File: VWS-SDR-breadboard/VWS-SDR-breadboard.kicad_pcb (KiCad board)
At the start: 4 copper layers, 47 x 30 mm, 78 parts, among them J1 RF_IN, J3 Conn_01x14, U1 GALI-S66, U2 74CBTLV3253DR, U3 MC33078, U4 MC33078, U5 AMS1117-3.3

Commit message: Board cleanup; Updated schematic info block
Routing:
- net GND: track 108.0 -> 106.9 mm
- net Net-(U3B--): track 15.1 -> 14.2 mm
- net Net-(C23-Pad1): track 17.4 -> 16.6 mm
- net Net-(U2-1B1): track 10.0 -> 9.25 mm
- net Net-(U2-1B2): track 8.26 -> 7.55 mm
- net Net-(U4A-+): track 13.2 -> 12.5 mm

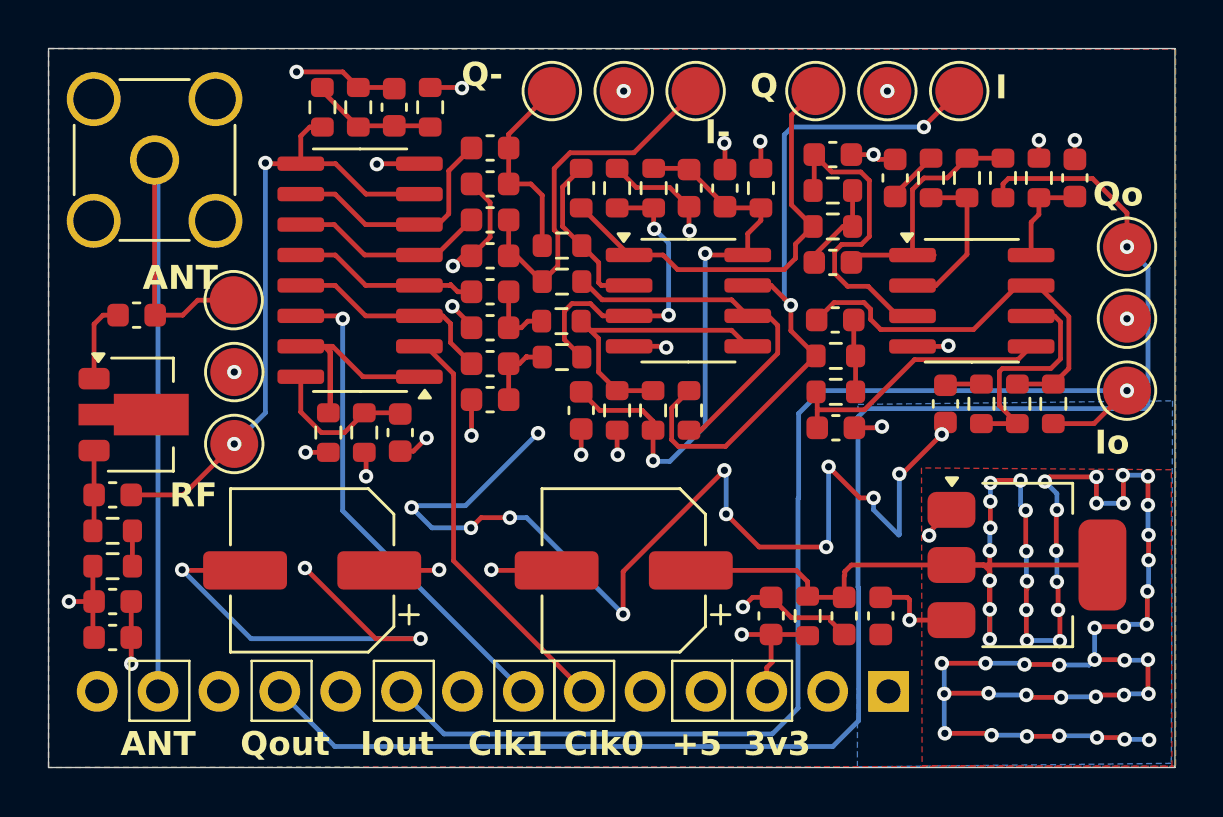
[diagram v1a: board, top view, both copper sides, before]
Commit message: v1.1: - Changed order of pins on the connector to simplify routing. I/Q should be closer to the power pins. clock should be closer to the antenna - Added GND fill on the Vcc layer under the antenna trace to the breadboard connector -Added ground stitching around the RF amp
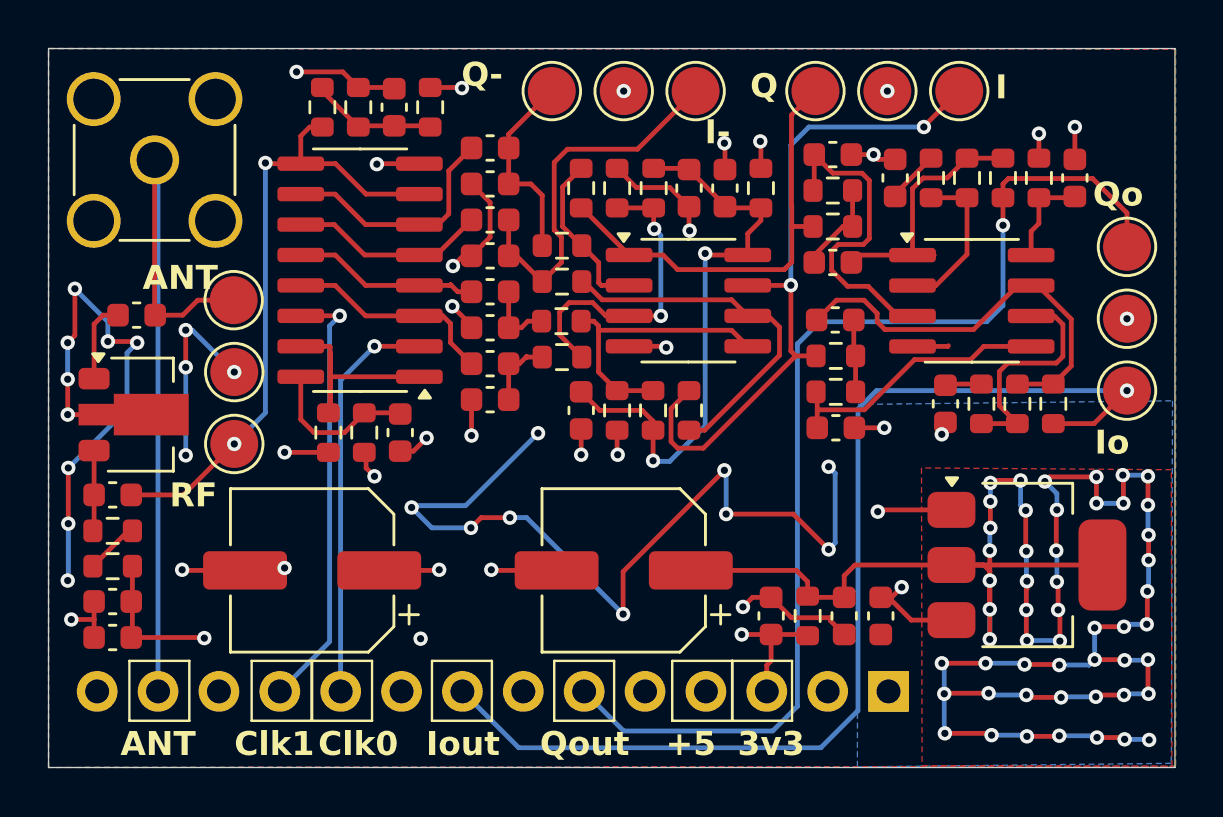
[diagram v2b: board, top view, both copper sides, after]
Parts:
- turned C2 to 0 degrees
- turned C3 to 0 degrees
- turned R1 to 180 degrees
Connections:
- J3 pad 10: GND -> /CLK0
- J3 pad 11: /Q_out -> /CLK1
- J3 pad 6: /CLK0 -> /Q_out
- J3 pad 7: /CLK1 -> GND
- J3 pad 8: GND -> /I_out
- J3 pad 9: /I_out -> GND
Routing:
- net /Q_out: track 65.4 -> 46.7 mm
- net GND: track 106.9 -> 113.4 mm, vias 39 -> 48
- net +5V: track 12.2 -> 15.1 mm
- net /CLK1: track 20.5 -> 18.3 mm
- net /I_out: track 47.8 -> 45.9 mm
- net /Ibb: track 30.0 -> 28.9 mm
- net Net-(U2-1~{OE}): track 12.0 -> 11.1 mm
- net Net-(L1-Pad1): track 1.47 -> 2.09 mm
- net Net-(U3B-+): track 12.4 -> 11.8 mm
- net /CLK0: track 17.1 -> 16.9 mm, vias 0 -> 1
- added copper zone on In2.Cu, net GND

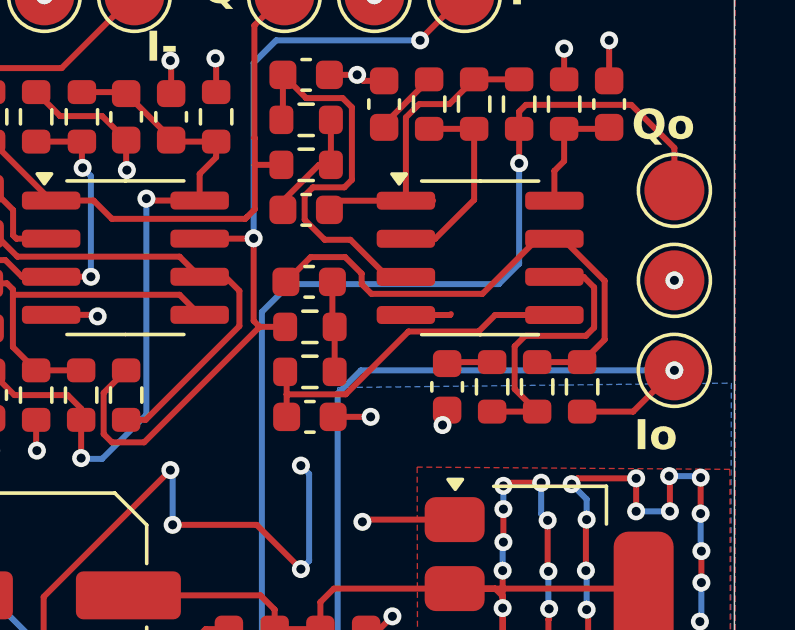
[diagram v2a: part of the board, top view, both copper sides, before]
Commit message: Added missing via to GND
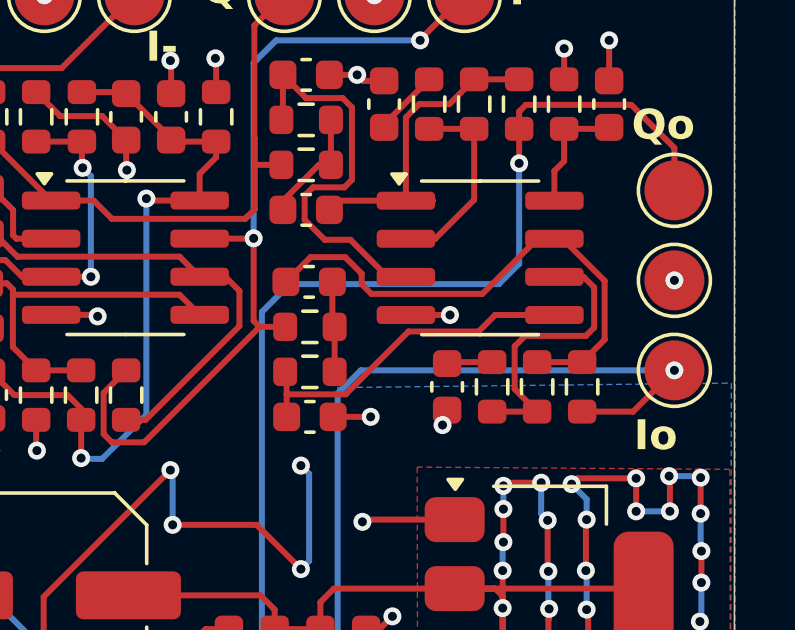
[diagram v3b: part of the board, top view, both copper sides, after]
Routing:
- net GND: vias 48 -> 49
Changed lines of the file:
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@@
+	)
+	(segment
+		(start 103.2 34.38)
+		(end 104.67 34.38)
+		(width 0.2)
+		(layer "F.Cu")
+		(net 3)
 	)
 	(segment
@@
 	)
 	(segment
-		(start 103.2 34.38)
-		(end 104.67 34.38)
-		(width 0.2)
-		(layer "F.Cu")
-		(net 3)
-	)
-	(segment
 		(start 86.4 41.525)
 		(end 85.2 41.525)
@@
 		(size 0.6)
 		(drill 0.3)
+		(layers "F.Cu" "B.Cu")
+		(net 3)
+	)
+	(via
+		(at 104.67 34.38)
+		(size 0.6)
+		(drill 0.3)
